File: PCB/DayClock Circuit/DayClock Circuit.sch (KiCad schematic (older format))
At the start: 41 parts, among them J1 molex 15-24-4441, J10 RGB_LED_Strip_Connector, J2 RJ45, J3 Conn_02x08_Odd_Even, J4 Conn_01x02, J5 Conn_01x03, J6 Conn_01x03, J7 Stepper Motor, J8 RGB_LED_Strip_Connector, J9 RGB_LED_Strip_Connector, Q1 N-MOSFET, Q2 N-MOSFET, Q3 N-MOSFET, Q4 N-MOSFET, Q5 N-MOSFET, Q6 N-MOSFET, Q7 N-MOSFET, Q8 N-MOSFET, Q9 N-MOSFET, SW1 SW_DIP_x03, U1 Arduino_Mega2560_Shield, U2 DRV8825_module, U3 Tiny_RTC_DS1307

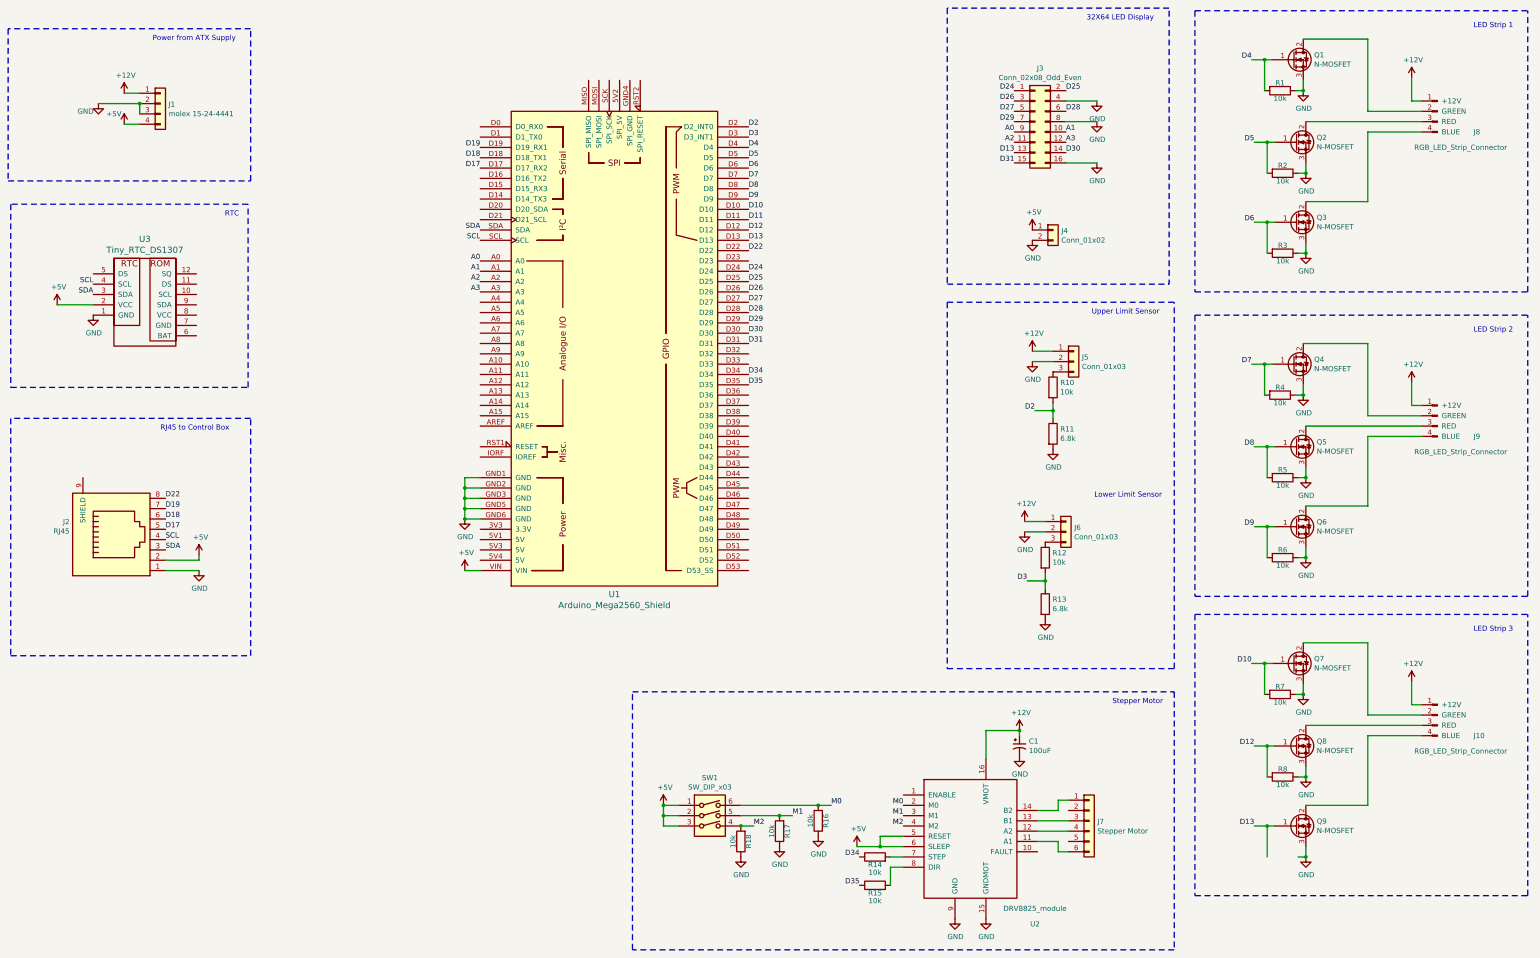
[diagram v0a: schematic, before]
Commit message: Added thick power traces and design rules.
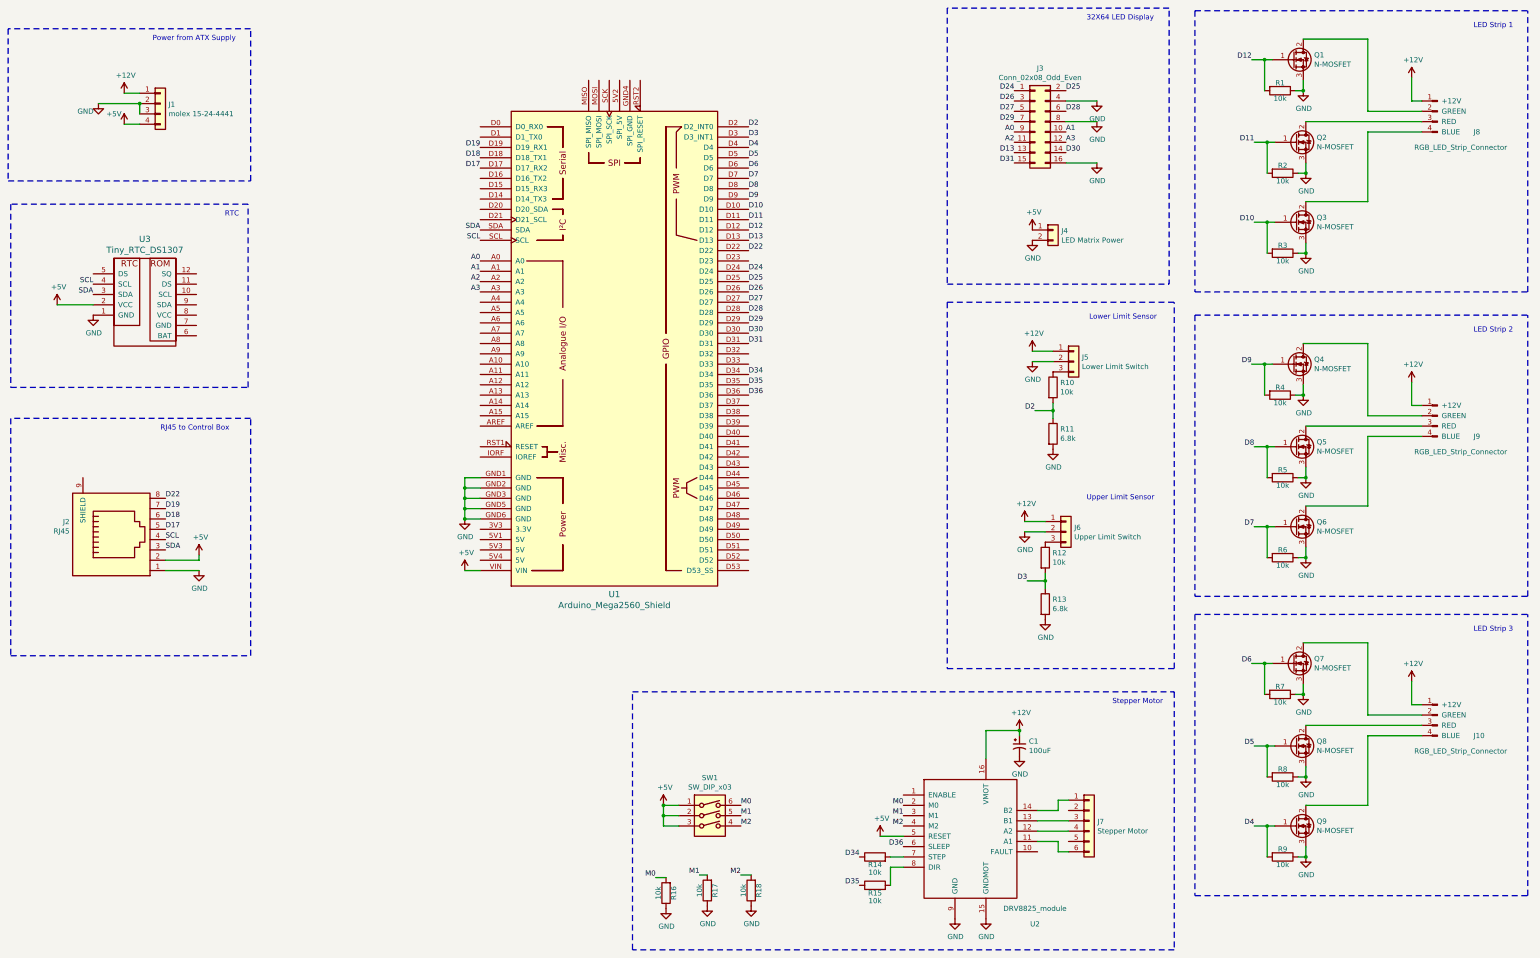
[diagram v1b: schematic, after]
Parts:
- added R9: 10k, Resistor_SMD:R_0805_2012Metric_Pad1.15x1.50mm_HandSolder, symbol Device:R
- J1: footprint TerminalBlock_Phoenix:TerminalBlock_Phoenix_MKDS-1,5-4-5.08_1x04_P5.08mm_Horizontal -> rich-footprints:Molex_15-24-4449_ATX_Power_Supply_Connector
- J3: footprint Connector_PinHeader_2.54mm:PinHeader_2x08_P2.54mm_Vertical -> rich-footprints:3M_Header_2x8_Keyed
- J4: value Conn_01x02 -> LED Matrix Power
- J5: value Conn_01x03 -> Lower Limit Switch
- J6: value Conn_01x03 -> Upper Limit Switch
- J7: footprint (none) -> Connector_JST:JST_XH_B06B-XH-A_1x06_P2.50mm_Vertical
- SW1: footprint (none) -> Button_Switch_THT:SW_DIP_SPSTx03_Slide_6.7x9.18mm_W7.62mm_P2.54mm_LowProfile
- U1: footprint Arduino:Arduino_Mega2560_Shield -> rich-footprints:Arduino_Mega2560_Shield_No_Serial_Header
- U2: footprint (none) -> rich-footprints:DRV8825_board
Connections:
- net +5V: no longer U2.6 (SLEEP)
- net D10: now also Q3.1 (G), R3.2; no longer Q7.1 (G), R7.2
- net D11: now also Q2.1 (G), R2.2
- net D12: now also Q1.1 (G), R1.2; no longer Q8.1 (G), R8.2
- net D13: no longer Q9.1 (G)
- net D4: now also Q9.1 (G), R9.2; no longer Q1.1 (G), R1.2
- net D5: now also Q8.1 (G), R8.2; no longer Q2.1 (G), R2.2
- net D6: now also Q7.1 (G), R7.2; no longer Q3.1 (G), R3.2
- net D7: now also Q6.1 (G), R6.2; no longer Q4.1 (G), R4.2
- net D9: now also Q4.1 (G), R4.2; no longer Q6.1 (G), R6.2
- net GND: now also R9.1
- net D36: now reaches U1.D36
- net D36: now also U2.6 (SLEEP)
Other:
- moved on the sheet: R16, R17, R18
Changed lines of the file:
@@
 F 0 "J3" H 11025 2317 50  0000 C CNN
 F 1 "Conn_02x08_Odd_Even" H 11025 2226 50  0000 C CNN
-F 2 "Connector_PinHeader_2.54mm:PinHeader_2x08_P2.54mm_Vertical" H 10975 1800 50  0001 C CNN
+F 2 "rich-footprints:3M_Header_2x8_Keyed" H 10975 1800 50  0001 C CNN
 F 3 "~" H 10975 1800 50  0001 C CNN
 	1    10975 1800
@@
 F 0 "U1" H 6900 1620 60  0000 C CNN
 F 1 "Arduino_Mega2560_Shield" H 6900 1514 60  0000 C CNN
-F 2 "Arduino:Arduino_Mega2560_Shield" H 7600 6750 60  0001 C CNN
+F 2 "rich-footprints:Arduino_Mega2560_Shield_No_Serial_Header" H 7600 6750 60  0001 C CNN
 F 3 "https://store.arduino.cc/arduino-mega-2560-rev3" H 7600 6750 60  0001 C CNN
 	1    6900 4000
@@
 P 11150 2850
 F 0 "J4" H 11230 2842 50  0000 L CNN
-F 1 "Conn_01x02" H 11230 2751 50  0000 L CNN
+F 1 "LED Matrix Power" H 11230 2751 50  0000 L CNN
 F 2 "TerminalBlock:TerminalBlock_Altech_AK300-2_P5.00mm" H 11150 2850 50  0001 C CNN
 F 3 "~" H 11150 2850 50  0001 C CNN
@@
 Text Label 10900 6250 2    50   ~ 0
 D3
-Text Label 13075 1200 2    50   ~ 0
+Text Label 13100 8625 2    50   ~ 0
 D4
-Text Label 13100 2000 2    50   ~ 0
+Text Label 13100 7850 2    50   ~ 0
 D5
-Text Label 13100 2775 2    50   ~ 0
+Text Label 13075 7050 2    50   ~ 0
 D6
-Text Label 13075 4150 2    50   ~ 0
+Text Label 13100 5725 2    50   ~ 0
 D7
 Text Label 13100 4950 2    50   ~ 0
 D8
-Text Label 13100 5725 2    50   ~ 0
+Text Label 13075 4150 2    50   ~ 0
 D9
-Text Label 13075 7050 2    50   ~ 0
+Text Label 13100 2775 2    50   ~ 0
 D10
 Text Label 10775 1500 2    50   ~ 0
@@
 F 0 "J1" H 2579 1617 50  0000 L CNN
 F 1 "molex 15-24-4441" H 2579 1526 50  0000 L CNN
-F 2 "TerminalBlock_Phoenix:TerminalBlock_Phoenix_MKDS-1,5-4-5.08_1x04_P5.08mm_Horizontal" H 2500 1625 50  0001 C CNN
+F 2 "rich-footprints:Molex_15-24-4449_ATX_Power_Supply_Connector" H 2500 1625 50  0001 C CNN
 F 3 "~" H 2500 1625 50  0001 C CNN
 	1    2500 1625
@@
 P 11350 4125
 F 0 "J5" H 11430 4167 50  0000 L CNN
-F 1 "Conn_01x03" H 11430 4076 50  0000 L CNN
+F 1 "Lower Limit Switch" H 11430 4076 50  0000 L CNN
 F 2 "Connector_JST:JST_XH_B03B-XH-A_1x03_P2.50mm_Vertical" H 11350 4125 50  0001 C CNN
 F 3 "~" H 11350 4125 50  0001 C CNN
@@
 Text Label 8200 2850 0    50   ~ 0
 D12
-Text Label 13100 8625 2    50   ~ 0
-D13
-Text Label 13100 7850 2    50   ~ 0
+Text Label 13075 1200 2    50   ~ 0
 D12
+Text Label 13100 2000 2    50   ~ 0
+D11
 $Comp
 L Device:R R10
@@
 	1    0    0    -1
 $EndComp
-Text Notes 11525 3675 0    50   ~ 0
+Text Notes 11475 5475 0    50   ~ 0
 Upper Limit Sensor
 $Comp
@@
 P 11275 5775
 F 0 "J6" H 11355 5817 50  0000 L CNN
-F 1 "Conn_01x03" H 11355 5726 50  0000 L CNN
+F 1 "Upper Limit Switch" H 11355 5726 50  0000 L CNN
 F 2 "Connector_JST:JST_XH_B03B-XH-A_1x03_P2.50mm_Vertical" H 11275 5775 50  0001 C CNN
 F 3 "~" H 11275 5775 50  0001 C CNN
@@
 	1    0    0    -1
 $EndComp
-Text Notes 11550 5450 0    50   ~ 0
+Text Notes 11500 3725 0    50   ~ 0
 Lower Limit Sensor
 $Comp
@@
 F 0 "U2" H 10975 7775 50  0000 C CNN
 F 1 "DRV8825_module" H 10975 7925 50  0000 C CNN
-F 2 "" H 10100 8675 50  0001 C CNN
+F 2 "rich-footprints:DRV8825_board" H 10100 8675 50  0001 C CNN
 F 3 "" H 10100 8675 50  0001 C CNN
 	1    10350 8675
@@
 F 0 "J7" H 11580 8567 50  0000 L CNN
 F 1 "Stepper Motor" H 11580 8476 50  0000 L CNN
-F 2 "" H 11500 8575 50  0001 C CNN
+F 2 "Connector_JST:JST_XH_B06B-XH-A_1x06_P2.50mm_Vertical" H 11500 8575 50  0001 C CNN
 F 3 "~" H 11500 8575 50  0001 C CNN
 	1    11500 8575
@@
 L power:+5V #PWR0136
 U 1 1 5B180805
-P 9250 8825
-F 0 "#PWR0136" H 9250 8675 50  0001 C CNN
-F 1 "+5V" H 9265 8998 50  0000 C CNN
-F 2 "" H 9250 8825 50  0001 C CNN
-F 3 "" H 9250 8825 50  0001 C CNN
-	1    9250 8825
+P 9475 8725
+F 0 "#PWR0136" H 9475 8575 50  0001 C CNN
+F 1 "+5V" H 9490 8898 50  0000 C CNN
+F 2 "" H 9475 8725 50  0001 C CNN
+F 3 "" H 9475 8725 50  0001 C CNN
+	1    9475 8725
 	1    0    0    -1
 $EndComp
@@
 F 0 "SW1" H 7825 9092 50  0000 C CNN
 F 1 "SW_DIP_x03" H 7825 9001 50  0000 C CNN
-F 2 "" H 7825 8625 50  0001 C CNN
+F 2 "Button_Switch_THT:SW_DIP_SPSTx03_Slide_6.7x9.18mm_W7.62mm_P2.54mm_LowProfile" H 7825 8625 50  0001 C CNN
 F 3 "" H 7825 8625 50  0001 C CNN
 	1    7825 8625
@@
 $EndComp
 Wire Wire Line
-	9700 8825 9475 8825
-Wire Wire Line
 	9700 8725 9475 8725
-Wire Wire Line
-	9475 8725 9475 8825
 $Comp
 L power:+5V #PWR0137
@@
 	7375 8625 7375 8525
 Connection ~ 7375 8525
-Wire Wire Line
-	9475 8825 9250 8825
-Connection ~ 9475 8825
 $Comp
 L Device:R R16
 U 1 1 5B212CFE
-P 8875 8575
-F 0 "R16" V 8800 8575 50  0000 C CNN
-F 1 "10k" V 8950 8575 50  0000 C CNN
-F 2 "Resistor_SMD:R_0805_2012Metric_Pad1.15x1.50mm_HandSolder" V 8805 8575 50  0001 C CNN
-F 3 "~" H 8875 8575 50  0001 C CNN
-	1    8875 8575
+P 7400 9275
+F 0 "R16" V 7325 9275 50  0000 C CNN
+F 1 "10k" V 7475 9275 50  0000 C CNN
+F 2 "Resistor_SMD:R_0805_2012Metric_Pad1.15x1.50mm_HandSolder" V 7330 9275 50  0001 C CNN
+F 3 "~" H 7400 9275 50  0001 C CNN
+	1    7400 9275
 	-1   0    0    1
 $EndComp
@@
 L power:GND #PWR0138
 U 1 1 5B212D05
-P 8875 8725
-F 0 "#PWR0138" H 8875 8475 50  0001 C CNN
-F 1 "GND" H 8880 8552 50  0000 C CNN
-F 2 "" H 8875 8725 50  0001 C CNN
-F 3 "" H 8875 8725 50  0001 C CNN
-	1    8875 8725
-	1    0    0    -1
-$EndComp
-Text Label 9000 8425 0    50   ~ 0
+P 7400 9425
+F 0 "#PWR0138" H 7400 9175 50  0001 C CNN
+F 1 "GND" H 7405 9252 50  0000 C CNN
+F 2 "" H 7400 9425 50  0001 C CNN
+F 3 "" H 7400 9425 50  0001 C CNN
+	1    7400 9425
+	1    0    0    -1
+$EndComp
+Text Label 8125 8425 0    50   ~ 0
 M0
 Text Label 9700 8425 2    50   ~ 0
@@
 Text Label 9700 8625 2    50   ~ 0
 M2
-Text Label 8625 8525 0    50   ~ 0
+Text Label 8125 8525 0    50   ~ 0
 M1
 $Comp
 L power:GND #PWR0139
 U 1 1 5B20D121
-P 8500 8825
-F 0 "#PWR0139" H 8500 8575 50  0001 C CNN
-F 1 "GND" H 8505 8652 50  0000 C CNN
-F 2 "" H 8500 8825 50  0001 C CNN
-F 3 "" H 8500 8825 50  0001 C CNN
-	1    8500 8825
-	1    0    0    -1
-$EndComp
-Wire Wire Line
-	8125 8525 8500 8525
-Wire Wire Line
-	8500 8525 8625 8525
-Connection ~ 8500 8525
+P 7800 9400
+F 0 "#PWR0139" H 7800 9150 50  0001 C CNN
+F 1 "GND" H 7805 9227 50  0000 C CNN
+F 2 "" H 7800 9400 50  0001 C CNN
+F 3 "" H 7800 9400 50  0001 C CNN
+	1    7800 9400
+	1    0    0    -1
+$EndComp
 $Comp
 L Device:R R17
 U 1 1 5B20D11A
-P 8500 8675
-F 0 "R17" V 8425 8675 50  0000 C CNN
-F 1 "10k" V 8575 8675 50  0000 C CNN
-F 2 "Resistor_SMD:R_0805_2012Metric_Pad1.15x1.50mm_HandSolder" V 8430 8675 50  0001 C CNN
-F 3 "~" H 8500 8675 50  0001 C CNN
-	1    8500 8675
+P 7800 9250
+F 0 "R17" V 7725 9250 50  0000 C CNN
+F 1 "10k" V 7875 9250 50  0000 C CNN
+F 2 "Resistor_SMD:R_0805_2012Metric_Pad1.15x1.50mm_HandSolder" V 7730 9250 50  0001 C CNN
+F 3 "~" H 7800 9250 50  0001 C CNN
+	1    7800 9250
 	-1   0    0    1
 $EndComp
-Wire Wire Line
-	8125 8625 8250 8625
-Text Label 8250 8625 0    50   ~ 0
+Text Label 8125 9100 2    50   ~ 0
 M2
 $Comp
 L power:GND #PWR0140
 U 1 1 5B1F6902
-P 8125 8925
-F 0 "#PWR0140" H 8125 8675 50  0001 C CNN
-F 1 "GND" H 8130 8752 50  0000 C CNN
-F 2 "" H 8125 8925 50  0001 C CNN
-F 3 "" H 8125 8925 50  0001 C CNN
-	1    8125 8925
-	1    0    0    -1
-$EndComp
-Connection ~ 8125 8625
+P 8225 9400
+F 0 "#PWR0140" H 8225 9150 50  0001 C CNN
+F 1 "GND" H 8230 9227 50  0000 C CNN
+F 2 "" H 8225 9400 50  0001 C CNN
+F 3 "" H 8225 9400 50  0001 C CNN
+	1    8225 9400
+	1    0    0    -1
+$EndComp
 $Comp
 L Device:R R18
 U 1 1 5B0C69E9
-P 8125 8775
-F 0 "R18" V 8050 8775 50  0000 C CNN
-F 1 "10k" V 8200 8775 50  0000 C CNN
-F 2 "Resistor_SMD:R_0805_2012Metric_Pad1.15x1.50mm_HandSolder" V 8055 8775 50  0001 C CNN
-F 3 "~" H 8125 8775 50  0001 C CNN
-	1    8125 8775
+P 8225 9250
+F 0 "R18" V 8150 9250 50  0000 C CNN
+F 1 "10k" V 8300 9250 50  0000 C CNN
+F 2 "Resistor_SMD:R_0805_2012Metric_Pad1.15x1.50mm_HandSolder" V 8155 9250 50  0001 C CNN
+F 3 "~" H 8225 9250 50  0001 C CNN
+	1    8225 9250
 	-1   0    0    1
 $EndComp
-Wire Wire Line
-	8125 8425 8875 8425
-Connection ~ 8875 8425
-Wire Wire Line
-	8875 8425 9000 8425
 Wire Notes Line
 	12325 7325 12325 9825
@@
 Text Notes 2500 4800 0    50   ~ 0
 RJ45 to Control Box
+$Comp
+L Device:R R9
+U 1 1 5B1D3C6F
+P 13375 8925
+F 0 "R9" V 13300 8925 50  0000 C CNN
+F 1 "10k" V 13450 8925 50  0000 C CNN
+F 2 "Resistor_SMD:R_0805_2012Metric_Pad1.15x1.50mm_HandSolder" V 13305 8925 50  0001 C CNN
+F 3 "~" H 13375 8925 50  0001 C CNN
+	1    13375 8925
+	0    1    1    0
+$EndComp
+Wire Wire Line
+	8125 9100 8225 9100
+Text Label 8125 8625 0    50   ~ 0
+M2
+Text Label 7725 9100 2    50   ~ 0
+M1
+Wire Wire Line
+	7725 9100 7800 9100
+Text Label 7300 9125 2    50   ~ 0
+M0
+Wire Wire Line
+	7300 9125 7400 9125
+Text Label 9700 8825 2    50   ~ 0
+D36
+Text Label 8200 4450 0    50   ~ 0
+D36
 $EndSCHEMATC

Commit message: Started on signal wires
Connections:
- net D10: now also Q9.1 (G), R9.2; no longer Q3.1 (G), R3.2
- net D11: now also Q8.1 (G), R8.2; no longer Q2.1 (G), R2.2
- net D12: now also Q7.1 (G), R7.2; no longer Q1.1 (G), R1.2
- net D4: now also Q3.1 (G), R3.2; no longer Q9.1 (G), R9.2
- net D5: now also Q2.1 (G), R2.2; no longer Q8.1 (G), R8.2
- net D6: now also Q1.1 (G), R1.2; no longer Q7.1 (G), R7.2
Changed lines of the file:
@@
 	13200 7050 13200 7350
-Wire Wire Line
-	13200 7050 13075 7050
-Connection ~ 13200 7050
 Wire Wire Line
 	13500 7350 13575 7350
@@
 Text Label 10900 6250 2    50   ~ 0
 D3
-Text Label 13100 8625 2    50   ~ 0
+Text Label 13100 2775 2    50   ~ 0
 D4
-Text Label 13100 7850 2    50   ~ 0
+Text Label 13100 2000 2    50   ~ 0
 D5
-Text Label 13075 7050 2    50   ~ 0
+Text Label 13075 1200 2    50   ~ 0
 D6
 Text Label 13100 5725 2    50   ~ 0
@@
 Text Label 13075 4150 2    50   ~ 0
 D9
-Text Label 13100 2775 2    50   ~ 0
+Text Label 13100 8625 2    50   ~ 0
 D10
 Text Label 10775 1500 2    50   ~ 0
@@
 Text Label 8200 2850 0    50   ~ 0
 D12
-Text Label 13075 1200 2    50   ~ 0
+Text Label 13075 7050 2    50   ~ 0
 D12
-Text Label 13100 2000 2    50   ~ 0
+Text Label 13100 7850 2    50   ~ 0
 D11
 $Comp
@@
 Text Label 8200 4450 0    50   ~ 0
 D36
+Wire Wire Line
+	13075 7050 13200 7050
+Connection ~ 13200 7050
 $EndSCHEMATC

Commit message: Giant Day Cycle Clock Rev 1A sent to fab and components ordered
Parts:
- added J11: Breakout Pins, Connector_PinHeader_2.54mm:PinHeader_1x10_P2.54mm_Vertical, symbol Connector_Generic:Conn_01x10
- U3: footprint rich-footprints:TinyRTC-one-mounting-hole -> rich-footprints:TinyRTC-coin-side-up
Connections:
- net +12V: now also J11.10 (Pin_10)
- net GND: now also J11.2 (Pin_2)
- net 5V3: now reaches U1.5V3 (5V)
- net 5V3: now also J11.1 (Pin_1)
- net D0: now reaches U1.D0 (D0_RX0)
- net D0: now also J11.8 (Pin_8)
- net D1: now reaches U1.D1 (D1_TX0)
- net D1: now also J11.9 (Pin_9)
- net D14: now reaches U1.D14 (D14_TX3)
- net D14: now also J11.7 (Pin_7)
- net D15: now reaches U1.D15 (D15_RX3)
- net D15: now also J11.6 (Pin_6)
- net D16: now reaches U1.D16 (D16_TX2)
- net D16: now also J11.5 (Pin_5)
- net D20: now reaches U1.D20 (D20_SDA)
- net D20: now also J11.4 (Pin_4)
- net D21: now reaches U1.D21 (D21_SCL)
- net D21: now also J11.3 (Pin_3)
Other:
- note added: "Breakout GPIO Pins"
- moved on the sheet: Q1, Q4, Q7, R1, R4, R7
